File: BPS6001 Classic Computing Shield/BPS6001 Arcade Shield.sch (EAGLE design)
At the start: 46 parts, among them J1 CON_PS/2, J2 CON_PS/2, J3 AUDIO-CONNECTOR-6P-SMD-344003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, U1 AMEGA_SHIELD_NOANALOGNO_ANALOG

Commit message: Major rework with all sections separated out.
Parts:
- removed AUDIO: AUDIOJACK, GadgetFactory:AUDIOJACK
- added AH1, AL: WING8WING8_NOHOLES, Papilio:WING8WING8_NOHOLES
- added C3, C4, C5, C6, C7: .1uF, GadgetFactory_6.0:C0805
- added IC1: MAX3232CSE, maxim:MAX3232CSE
- added R21: 47K, GadgetFactory:R0603
- added R22: 3.3K, GadgetFactory:R0603
- added R23, R24, R25: 50K, GadgetFactory_6.0:R0805
- added R26, R27, R43, R44: 390, GadgetFactory:R0603
- added R33, R37, R40: 1K, GadgetFactory:R0603
- added R34, R38, R39: 510, GadgetFactory:R0603
- added R35, R42: 3.9K, GadgetFactory:R0603
- added R36, R41: 2K, GadgetFactory:R0603
- added SP1: (no value), con-subd:M09HP
- C1, C2: device resistor:C-EU050-025X075 -> GadgetFactory:C0603
- J2: value CON_PS/2 -> AUDIO-CONNECTOR-6P-SMD-3440030P1; device usb1:CON_PS/2 -> OPL Eagle Library:AUDIO-CONNECTOR-6P-SMD-3440030P1
- J3: value AUDIO-CONNECTOR-6P-SMD-3440030P1 -> CON_PS/2; device OPL Eagle Library:AUDIO-CONNECTOR-6P-SMD-3440030P1 -> usb1:CON_PS/2
- R1, R2: value 82.5 -> 47K
- R10, R11, R6: value 510 -> 47K
- R12, R5, R9: value 1K -> 47K
- R13, R4, R8: value 2K -> 47K
- R14, R3, R7: value 3.9K -> 47K
- R16, R19: value 3.3K -> 47K
- R28: value 47K -> 3.3K
- R29, R30: value 390 -> 82.5
- R31: value 390 -> 3.9K
- R32: value 390 -> 2K
- X1: device con-subd:F15HDH -> GadgetFactory_6.0:F15HDH
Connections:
- removed net AUDIO+: C2.1, R19A.2, U1.*D20
- removed net AUDIO-: C1.1, R16A.2, U1.*D19
- removed net N$1: J3.L, R16A.1
- removed net N$16: JS2.1
- removed net N$17: JS2.2
- removed net N$18: JS2.3
- removed net N$21: JS2.9
- removed net NC1: U1.D4
- removed net NC2: U1.*D3
- removed net SD_DI: SD1.DATA_IN
- removed net SD_DO: SD1.DATA_OUT
- removed net SW1: R15A.2, S1.P, S1.P1, U1.*D2
- removed net SW2: R18A.2, S2.P, S2.P1, U1.D15
- removed net SW3: R17A.2, S3.P, S3.P1, U1.D16
- removed net SW4: R20A.2, S4.P, S4.P1, U1.D17
- new net 5V0_PS2: AH1.5V, J3.VCC
- new net AUDIO-LEFT: R22A.2, U1.D28
- new net AUDIO-RIGHT: R28A.2, U1.D30
- new net CTS: IC1G$1.R2OUT
- new net DTE_CTS: IC1G$1.R2IN, SP1.8
- new net DTE_RTS: IC1G$1.T2OUT, SP1.7
- new net DTE_RX: IC1G$1.R1IN, SP1.2
- new net DTE_TX: IC1G$1.T1OUT, SP1.3
- new net JOY_3V3: AH1.3V3, AL.3V3, R12A.2, R13A.2, R14A.2, R15A.2, R16A.2, R19A.2, R20A.2, R21A.2
- new net JOY_GND: AH1.GND, AL.GND, J3.GND, JS2.8, LED1.C, LED2.C, LED3.C, LED4.C, U1.GND@4
- new net JS1_1: JS1.1, R1A.1, U1.D13
- new net JS1_2: JS1.2, R3A.1, U1.D11
- new net JS1_3: JS1.3, R5A.1, U1.D9
- new net JS1_4: JS1.4, R6A.1, U1.D8
- new net JS1_5: JS1.5, R8A.1, U1.D6
- new net JS1_6: JS1.6, R2A.1, U1.D12
- new net JS1_7: JS1.7, R4A.1, U1.D10
- new net JS1_9: JS1.9, R7A.1, U1.D7
- new net JS2_7: AL.2, JS2.7, R20A.1, U1.D35
- new net LED5: AH1.2, U1.D51
- new net LED6: AH1.1, U1.D53
- new net N$12: C4.2, IC1G$1.C2+
- new net N$13: C5.1, IC1G$1.C1-
- new net N$14: C4.1, IC1G$1.C2-
- new net N$34: C2.1, J2.R, R28A.1
- new net N$6: C6.1, IC1G$1.V+
- new net N$7: C3.1, IC1G$1.V-
- new net N$8: C5.2, IC1G$1.C1+
- new net RTS: IC1G$1.T2IN
- new net SD_CD: SD1.CARD_DETECT, U1.*D3
- new net SD_MISO: R23A.1, SD1.DATA_OUT, U1.*D2
- new net SD_MOSI: R24A.1, SD1.DATA_IN, U1.D14
- new net SW_DOWN: R17A.2, S4.P, S4.P1, U1.*D20
- new net SW_LEFT: R9A.2, S3.P, S3.P1, U1.D17
- new net SW_RIGHT: R18A.2, S5.P, S5.P1, U1.*D21
- new net SW_UP: R10A.2, S1.P, S1.P1, U1.*D18
- net 3V3: now also C7.1, IC1P.VCC, R1A.2, R23A.2, R24A.2, R25A.2, R2A.2, R3A.2, R4A.2, R5A.2, R6A.2, R7A.2, R8A.2
- net 5V0: no longer J2.VCC, JS1.7, U1.5V@1
- net BLUE: now also R31A.2, R32A.2, R33A.2, R34A.2; no longer R3A.2, R4A.2, R5A.2, R6A.2
- net BLUE1: now also R31A.1, U1.D26; no longer R3A.1, U1.D30
- net BLUE2: now also R32A.1; no longer R4A.1
- net BLUE3: now also R33A.1; no longer R5A.1
- net BLUE4: now also R34A.1; no longer R6A.1
- net GND: now also C3.2, C6.2, C7.2, IC1P.GND, J2.COM1, J2.COM2, R10A.1, R11A.1, R9A.1, SP1.5, SP1.G1, SP1.G2; no longer AUDIO.1, J2.GND, LED1.C, LED2.C, LED3.C, LED4.C, R15A.1, R20A.1, R28A.1, U1.GND@4
- net GREEN: now also R35A.2, R36A.2, R37A.2, R38A.2; no longer R10A.2, R7A.2, R8A.2, R9A.2
- net GREEN1: now also R35A.1; no longer R7A.1
- net GREEN2: now also R36A.1; no longer R8A.1
- net GREEN3: now also R37A.1; no longer R9A.1
- net GREEN4: now also R38A.1; no longer R10A.1
- net HORIZONTAL_SYNC: now also R29A.1, U1.D22; no longer R1A.1, U1.*D21
- net JS2_1: now also AL.4, JS2.1, R16A.1, U1.D31; no longer JS1.1, U1.D13
- net JS2_2: now also AL.5, JS2.2, R15A.1, U1.D29; no longer JS1.2, U1.D11
- net JS2_3: now also AL.6, JS2.3, R14A.1, U1.D27; no longer JS1.3, U1.D10
- net JS2_4: now also AL.7, JS2.4, R13A.1, U1.D25; no longer JS1.4, U1.D9
- net JS2_5: now also AL.8, JS2.5, R12A.1, U1.D23; no longer JS1.5, U1.D7
- net JS2_6: now also AL.3, JS2.6, R19A.1, U1.D33; no longer JS1.6, U1.D12
- net JS2_9: now also AL.1, JS2.9, R21A.1, U1.D37; no longer JS1.9, U1.D8
- net LED1: now also AH1.6, R26A.2, U1.D43; no longer R29A.2, U1.D22
- net LED2: now also AH1.5, R27A.2, U1.D45; no longer R30A.2, U1.D24
- net LED3: now also AH1.4, R43A.2, U1.D47; no longer R31A.2, U1.D26
- net LED4: now also AH1.3, R44A.2, U1.D49; no longer R32A.2, U1.D28
- net N$10: now also R27A.1; no longer R30A.1
- net N$11: now also R26A.1; no longer R29A.1
- net N$2: now also C1.1, J2.L, R22A.1; no longer J3.R, R19A.1
- net N$3: now also R44A.1; no longer R32A.1
- net N$4: now also R29A.2; no longer R1A.2
- net N$5: now also R30A.2; no longer R2A.2
- net N$9: now also R43A.1; no longer R31A.1
- net PS2CLK1: now also U1.D5; no longer U1.D6
- net PS2CLK2: now also AH1.8, J3.CLK, U1.D39; no longer J2.CLK
- net PS2DAT1: now also U1.D4; no longer U1.D5
- net PS2DAT2: now also AH1.7, J3.DATA, U1.D41; no longer J2.DATA
- net RED: now also R39A.2, R40A.2, R41A.2, R42A.2; no longer R11A.2, R12A.2, R13A.2, R14A.2
- net RED1: now also R42A.1; no longer R14A.1
- net RED2: now also R41A.1; no longer R13A.1
- net RED3: now also R40A.1; no longer R12A.1
- net RED4: now also R39A.1; no longer R11A.1
- net RESET: now also R11A.2, S2.P, S2.P1, U1.*D19; no longer R28A.2, S5.P, S5.P1, U1.*D18
- net RX: now also IC1G$1.R1OUT; no longer JS2.5
- net SD_!CS: now also R25A.1, U1.D16
- net SD_SCK: now also U1.D15
- net TX: now also IC1G$1.T1IN; no longer JS2.4
- net VERTICAL_SYNC: now also R30A.1, U1.D24; no longer R2A.1, U1.D14
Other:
- note added: "Copyright 2010-2012 Gadget Factory, LLC"
- note added: "TODO: Add Jumpers to buttons TODO: Put buttons on Joystick pins? TODO: Add Grove Connector TODO: Change silkscreen of the buttons TODO: Consider adding thumb joystick"
- note added: "This work is licensed under the Creative Commons Non-Commercial Attribution Share-Alike License."
- note removed: "TODO: Check spacing on ps/2 ports"

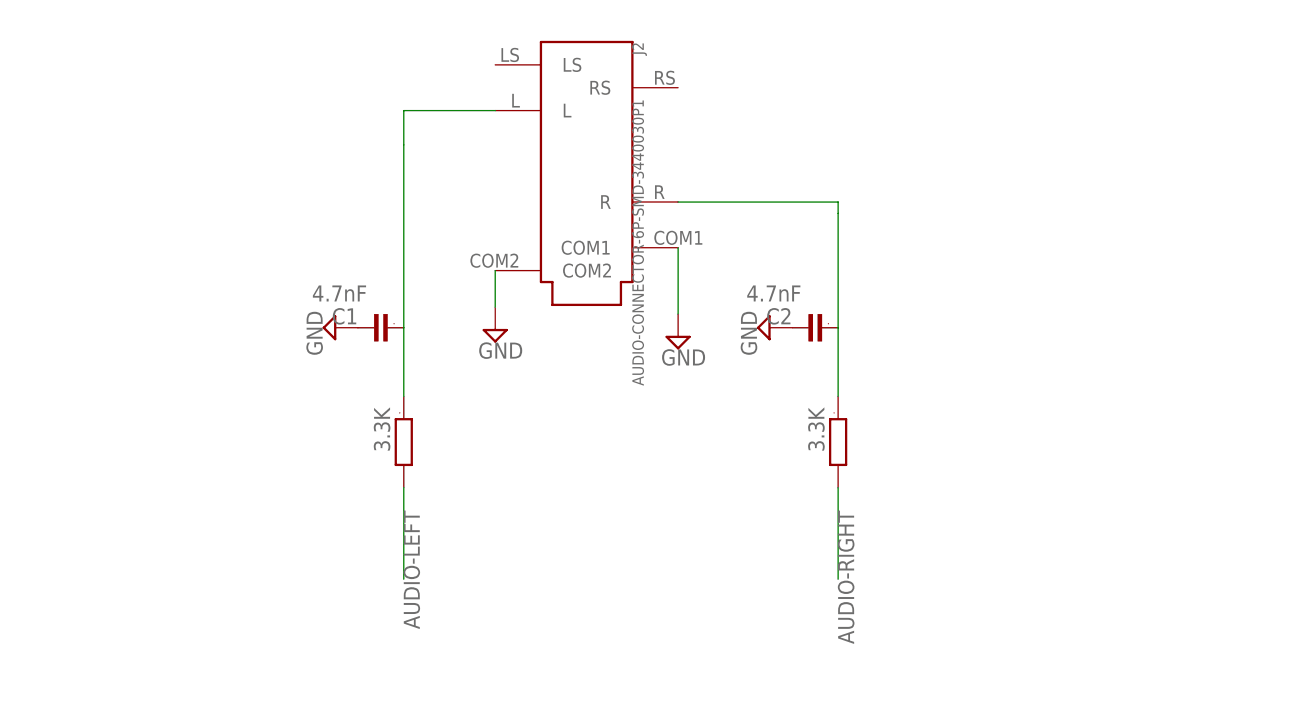
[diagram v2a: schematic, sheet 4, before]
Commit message: 2nd Audio Jack, Mounting Holes
Moved the Joystick ports to the same side, I'm considering rotating the
whole thing 180 degrees so the joysticks are on the bottom...
Added a second audio jack to the 16 bit Wing.
The first audio jack is now connected to the Analog input pins of the
atmel chip and also to FPGA pins. This is for reading data off tape
drives or recording audio.
Added mounting holes.
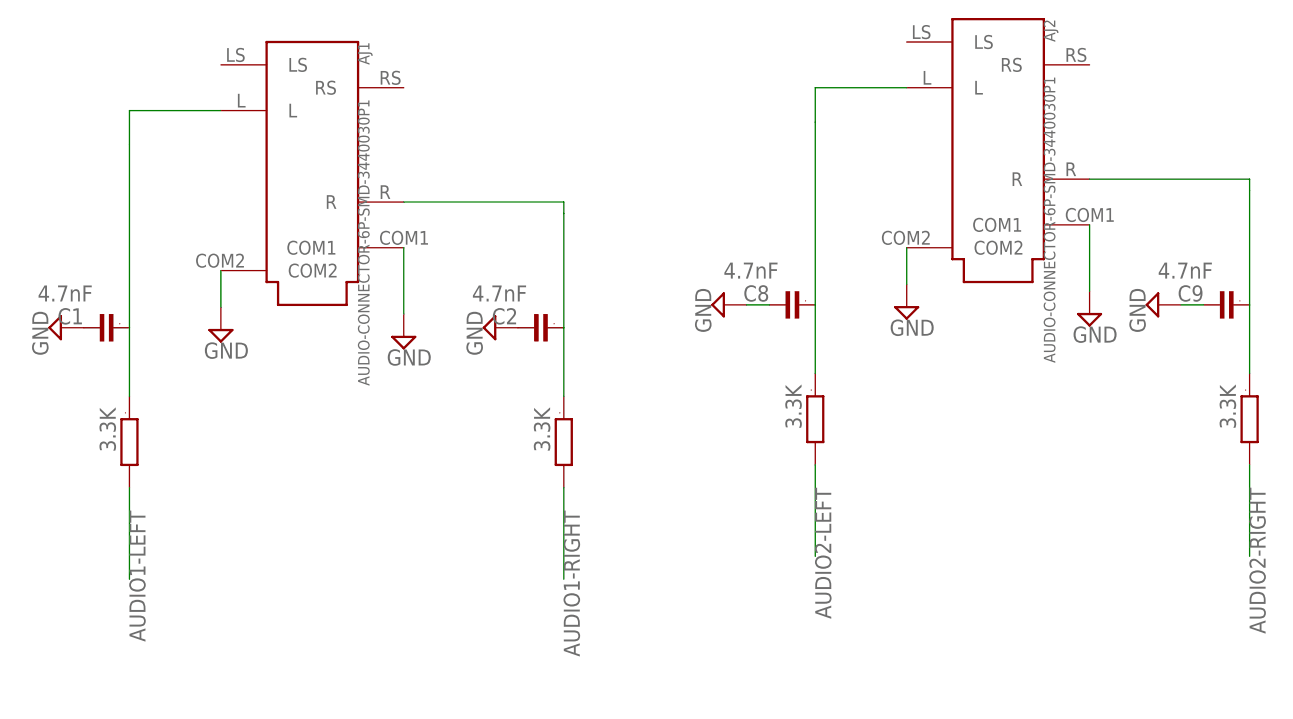
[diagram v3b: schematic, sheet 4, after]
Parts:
- removed AH1, AL: WING8WING8_NOHOLES, Papilio:WING8WING8_NOHOLES
- removed J2: AUDIO-CONNECTOR-6P-SMD-3440030P1, OPL Eagle Library:AUDIO-CONNECTOR-6P-SMD-3440030P1
- added AJ1, AJ2: AUDIO-CONNECTOR-6P-SMD-3440030P1, OPL Eagle Library:AUDIO-CONNECTOR-6P-SMD-3440030P1
- added C8, C9: 4.7nF, GadgetFactory:C0603
- added PWR_1, PWR_2: POWER_ONLYNOTEXT, Papilio:POWER_ONLYNOTEXT
- added R45, R46: 3.3K, GadgetFactory:R0603
- added R47, R48: 390, GadgetFactory_6.0:R0603
- renumbered J1 to PS2_A, J3 to PS2_B
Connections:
- net AUDIO-LEFT renamed AUDIO1-LEFT
- net AUDIO-RIGHT renamed AUDIO1-RIGHT
- removed net LED5: AH1.2, U1.D51
- removed net LED6: AH1.1, U1.D53
- new net AUDIO2-LEFT: R45A.2, U1.D45
- new net AUDIO2-RIGHT: R46A.2, U1.D43
- new net N$1: AJ2.L, C8.1, R45A.1
- new net N$15: AJ2.R, C9.1, R46A.1
- new net N$16: PS2_B.DATA, R47A.2
- new net N$17: PS2_B.CLK, R48A.2
- net 5V0_PS2: now also PWR_2.5V0@P4; no longer AH1.5V
- net GND: now also AJ1.COM1, AJ1.COM2; no longer J2.COM1, J2.COM2
- net JOY_3V3: now also PWR_1.3V3@P3; no longer AH1.3V3, AL.3V3
- net JOY_GND: now also AJ2.COM1, AJ2.COM2, C8.2, C9.2, PWR_1.GND@P1, PWR_2.GND@P1; no longer AH1.GND, AL.GND
- net JS2_1: no longer AL.4
- net JS2_2: no longer AL.5
- net JS2_3: no longer AL.6
- net JS2_4: no longer AL.7
- net JS2_5: no longer AL.8
- net JS2_6: no longer AL.3
- net JS2_7: no longer AL.2
- net JS2_9: no longer AL.1
- net LED1: now also U1.D47; no longer AH1.6, U1.D43
- net LED2: now also U1.D49; no longer AH1.5, U1.D45
- net LED3: now also U1.D51; no longer AH1.4, U1.D47
- net LED4: now also U1.D53; no longer AH1.3, U1.D49
- net N$2: now also AJ1.L; no longer J2.L
- net N$34: now also AJ1.R; no longer J2.R
- net PS2CLK2: now also R48A.1; no longer AH1.8, PS2_B.CLK
- net PS2DAT2: now also R47A.1; no longer AH1.7, PS2_B.DATA
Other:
- moved on the sheet: C1, C2
